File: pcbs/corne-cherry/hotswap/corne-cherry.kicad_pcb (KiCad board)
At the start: 2 copper layers, 277.2 x 107.5 mm, 180 parts, among them J1 TYPE-C-31-M-13C, J2 TRS, J3 Conn_01x04, J4 Conn_01x03, SW1 SW_Push, SW10 SW_Push, SW11 SW_Push, SW12 SW_Push, SW13 SW_Push, SW14 SW_Push, SW15 SW_Push, SW16 SW_Push, SW17 SW_Push, SW18 SW_Push, SW19 SW_Push, SW2 SW_Push, SW20 SW_Push, SW21 SW_Push, SW3 SW_Push, SW4 SW_Push, SW5 SW_Push, SW6 SW_Push, SW7 SW_Push, SW8 SW_Push, SW9 SW_Push, U1 RP2040, U2 NCP1117LPST33T3G, U3 TPD4E05U06DQAR, U4 W25Q128JVSIQ, Y1 12MHz 18pF

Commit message: add keys and LEDs
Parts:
- removed G*** (x2): LOGO, kbd_local:corne-logo-horizontal
- added LED22: YS-SK6812MINI-E, kbd_local:YS-SK6812MINI-E, B.Cu at (86.6, -61.2)
- added LED23: YS-SK6812MINI-E, kbd_local:YS-SK6812MINI-E, B.Cu at (105.7, -61.2)
- added LED24: YS-SK6812MINI-E, kbd_local:YS-SK6812MINI-E, B.Cu at (124.7, -61.2)
- added SW22: SW_Push, kbd:keyswitch_cherrymx_hotswap_1u, B.Cu at (86.6, -66.0)
- added SW23: SW_Push, kbd:keyswitch_cherrymx_hotswap_1u, B.Cu at (105.7, -66.0)
- added SW24: SW_Push, kbd:keyswitch_cherrymx_hotswap_1u, B.Cu at (124.7, -66.0)
- added rLED22: YS-SK6812MINI-E, kbd_local:YS-SK6812MINI-E, B.Cu at (343.8, -61.2)
- added rLED23: YS-SK6812MINI-E, kbd_local:YS-SK6812MINI-E, B.Cu at (324.8, -61.2)
- added rLED24: YS-SK6812MINI-E, kbd_local:YS-SK6812MINI-E, B.Cu at (305.7, -61.2)
- added rSW22: SW_Push, kbd:keyswitch_cherrymx_hotswap_1u, B.Cu at (343.8, -66.0)
- added rSW23: SW_Push, kbd:keyswitch_cherrymx_hotswap_1u, B.Cu at (324.8, -66.0)
- added rSW24: SW_Push, kbd:keyswitch_cherrymx_hotswap_1u, B.Cu at (305.7, -66.0)
- moved BT3 19.1 mm to (86.6, -55.8)
- moved BT4 19.1 mm to (105.7, -55.8)
- moved rBT3 19.1 mm to (343.8, -55.8)
- moved rBT4 19.1 mm to (324.8, -55.8)
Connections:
- net /left/KEYEX1 renamed /left/KEY22
- net /left/KEYEX2 renamed /left/KEY23
- net /left/RE0A renamed /left/KEY24
- net /right/KEYEX1 renamed /right/KEY22
- net /right/KEYEX2 renamed /right/KEY23
- net /right/RE0A renamed /right/KEY24
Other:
- outline, holes or cut-outs redrawn

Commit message: add LEDs wiring
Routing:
- net Net-(rD1-K): track 537.7 -> 615.5 mm, vias 34 -> 37
- net Net-(D1-K): track 536.4 -> 612.9 mm, vias 36 -> 39
- net Net-(LED23-DOUT): track 0.00 -> 28.2 mm
- net Net-(LED22-DOUT): track 0.00 -> 28.1 mm
- net Net-(rEXLED1-DIN): track 224.0 -> 244.8 mm
- net Net-(EXLED1-DIN): track 222.7 -> 242.7 mm
- net Net-(rLED23-DOUT): track 0.00 -> 14.0 mm
- net Net-(rLED22-DOUT): track 0.00 -> 14.0 mm
- net GNDR: vias 71 -> 77
- net GND: vias 69 -> 75
- net /right/KEY23: vias 2 -> 3
- net /right/KEY22: vias 0 -> 1
- net /left/KEY23: vias 2 -> 3
- net /left/KEY22: vias 2 -> 3

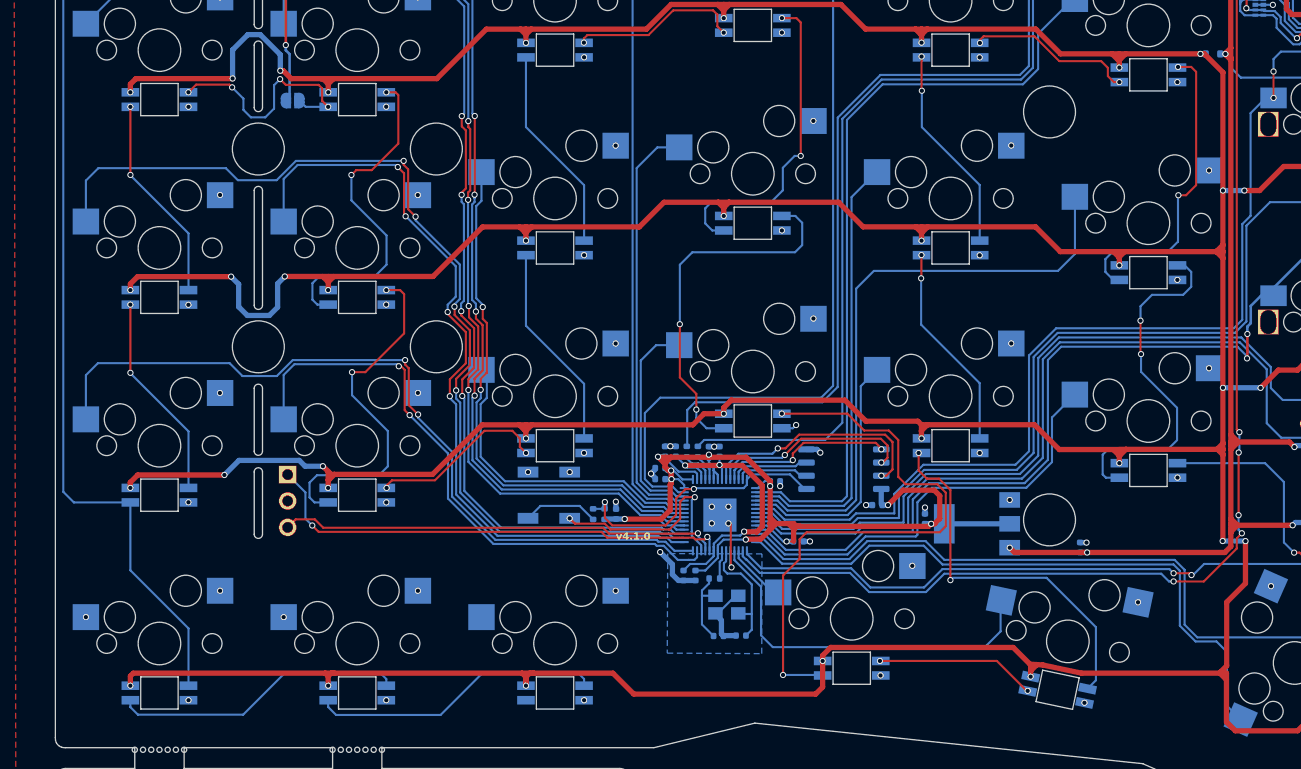
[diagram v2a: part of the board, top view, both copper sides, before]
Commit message: add left keys wiring
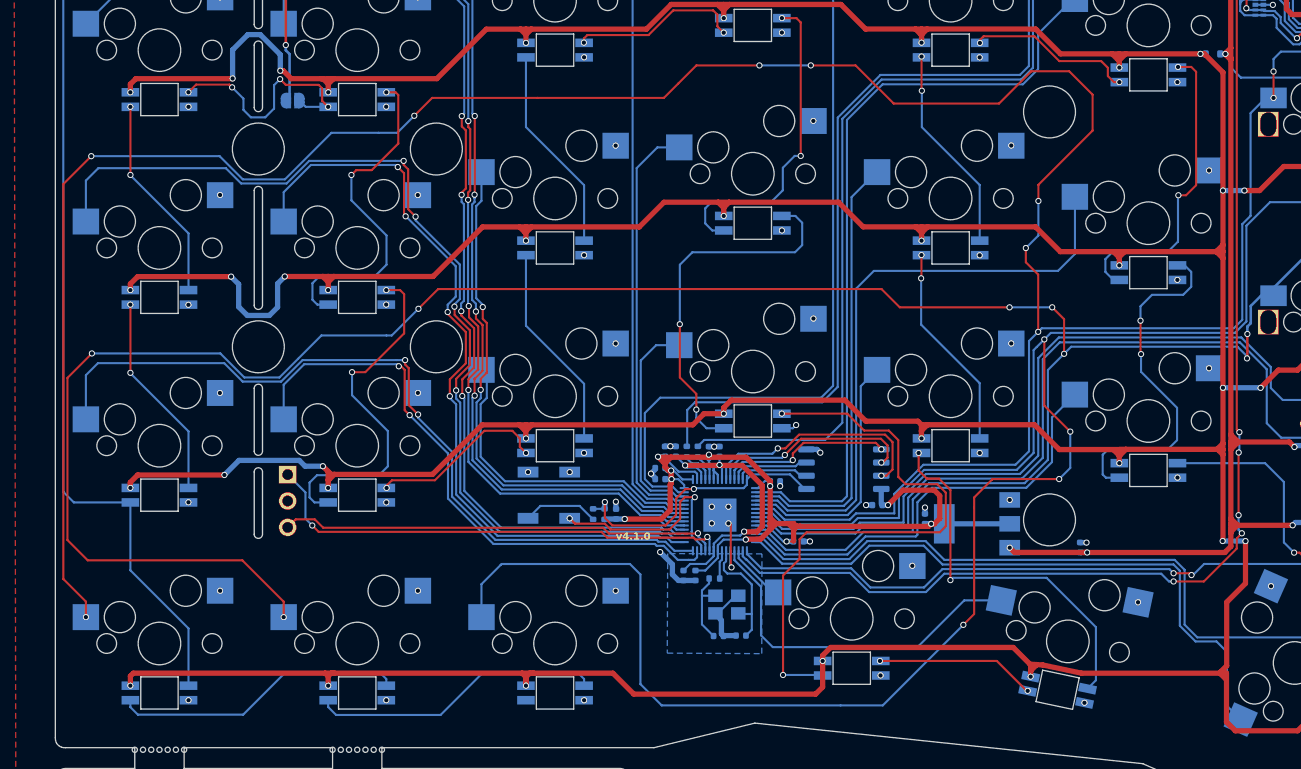
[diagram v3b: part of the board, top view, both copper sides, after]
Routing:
- net /left/KEY22: track 93.6 -> 272.5 mm, vias 3 -> 10
- net /left/KEY23: track 79.1 -> 224.9 mm, vias 3 -> 8
- net /left/KEY24: track 79.8 -> 182.2 mm, vias 0 -> 4
- net /left/KEY8: track 36.4 -> 34.7 mm
- net /left/KEY17: track 75.4 -> 74.7 mm
- net /left/KEY16: track 57.9 -> 57.3 mm
